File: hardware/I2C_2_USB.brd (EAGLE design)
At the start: 14.9 x 20.3 mm, 14 parts, among them CN1 1X4-BIG, J3 USB-MICROB, U1 ATMEGA328P-MU-QFN32

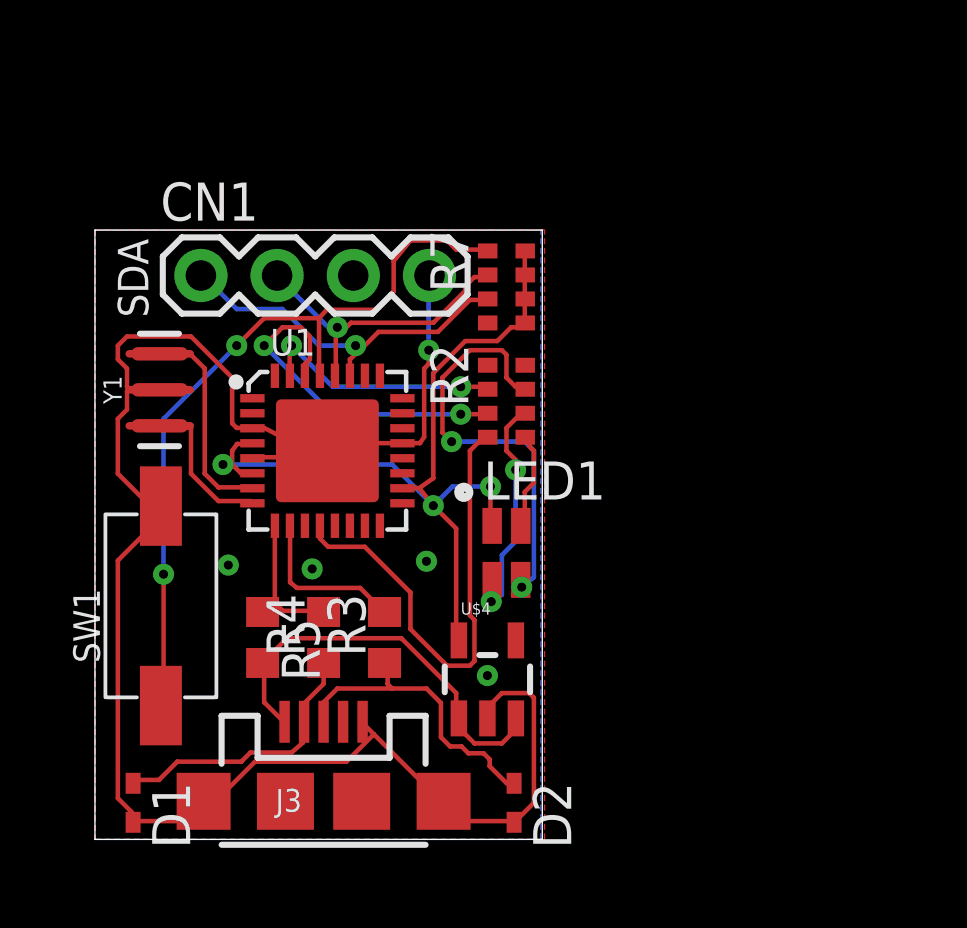
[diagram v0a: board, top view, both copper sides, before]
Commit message: Connect SDA and TxD Lines
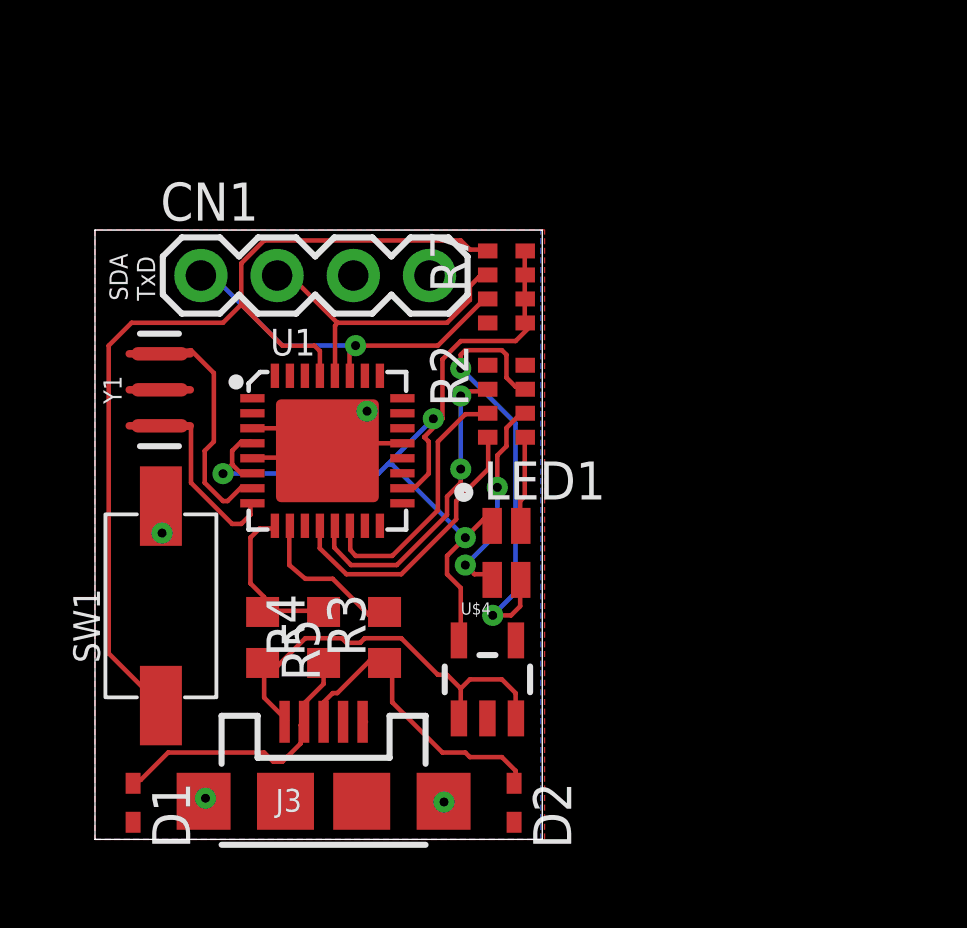
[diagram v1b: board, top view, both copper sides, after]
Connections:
- net LED renamed LED_RED
- removed net ADCENA: U1.13
- removed net OUTA: U1.14
- new net LED_BLUE: R2.3, U1.14
- new net LED_GREEN: R2.2, U1.13
- net RXD: no longer R2.3
- net TXD: no longer R2.2
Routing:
- net GND: track 60.3 -> 10.1 mm, vias 5 -> 4
- net RXD: track 11.7 -> 0.00 mm, vias 2 -> 0
- net LED_GREEN: track 0.00 -> 10.6 mm, vias 0 -> 2
- net LED_BLUE: track 0.00 -> 8.78 mm
- net TXD: track 8.29 -> 0.00 mm, vias 2 -> 0
- net LED_RED: track 16.0 -> 9.61 mm
- net RST: track 25.9 -> 31.9 mm, vias 2 -> 0
- net XTAL1: track 6.98 -> 7.95 mm
- net XTAL2: track 5.03 -> 5.96 mm
- net BLUE: track 7.87 -> 7.12 mm
- net +3V3: track 29.9 -> 30.4 mm
- net SCL: track 10.2 -> 10.4 mm, vias 1 -> 0
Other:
- board text added: "SDA TxD"
- board text removed: "SDA"

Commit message: Add crypto module & backside labels
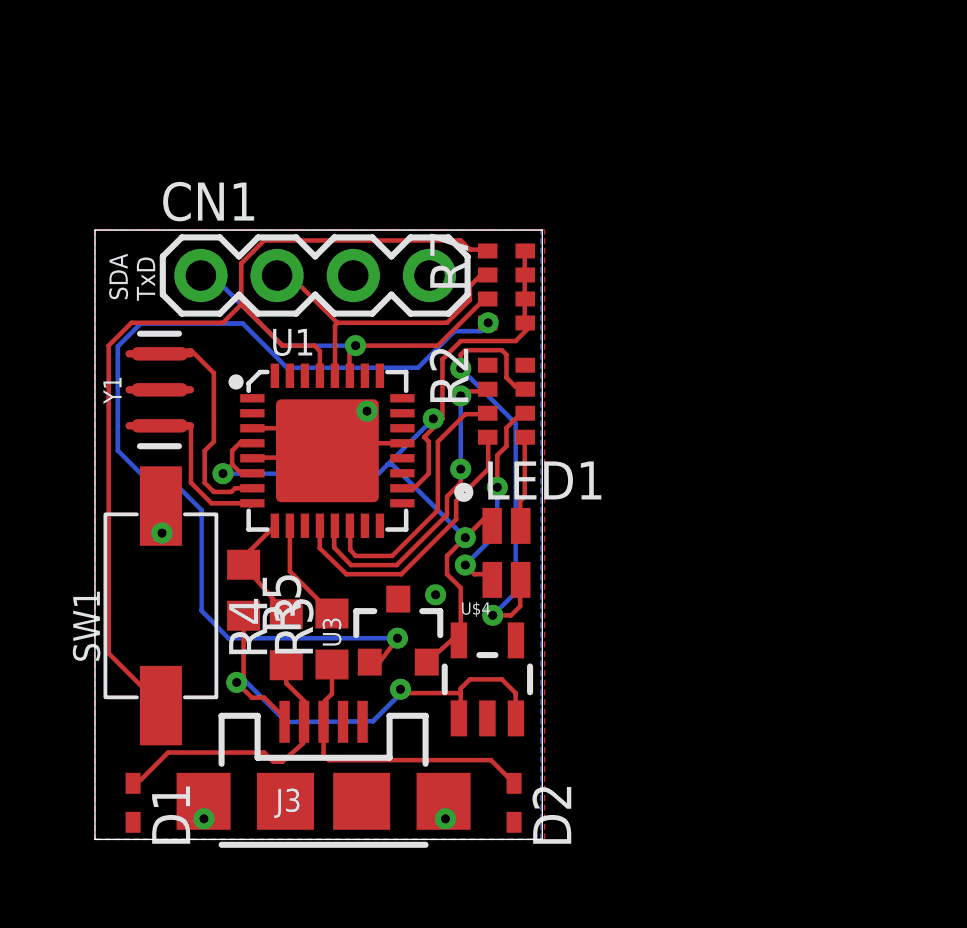
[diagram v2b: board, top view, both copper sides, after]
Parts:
- added U3: ATSHA204-TSU, SparkFun-IC-Special-Function:SOT23-3
- moved R3 1.75 mm to (7.90, 6.68)
- moved R5 1.70 mm to (4.95, 8.31)
- moved R4 1.25 mm to (6.38, 6.65)
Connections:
- new net CRYPTO: R7.4, U3.1
- net +3V3: now also U3.2
- net GND: now also U3.3
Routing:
- net CRYPTO: track 0.00 -> 33.0 mm, vias 0 -> 2
- net +5V: track 14.1 -> 17.2 mm, vias 0 -> 2
- net D-: track 5.71 -> 3.91 mm
- net D+: track 5.23 -> 3.50 mm
- net +3V3: track 30.4 -> 31.8 mm
- net XTAL2: track 5.96 -> 5.30 mm
- net GND: track 10.1 -> 9.46 mm, vias 4 -> 5
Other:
- board text added: "3V3"
- board text added: "GND"
- board text added: "SCL RxD"

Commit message: Add BLE module
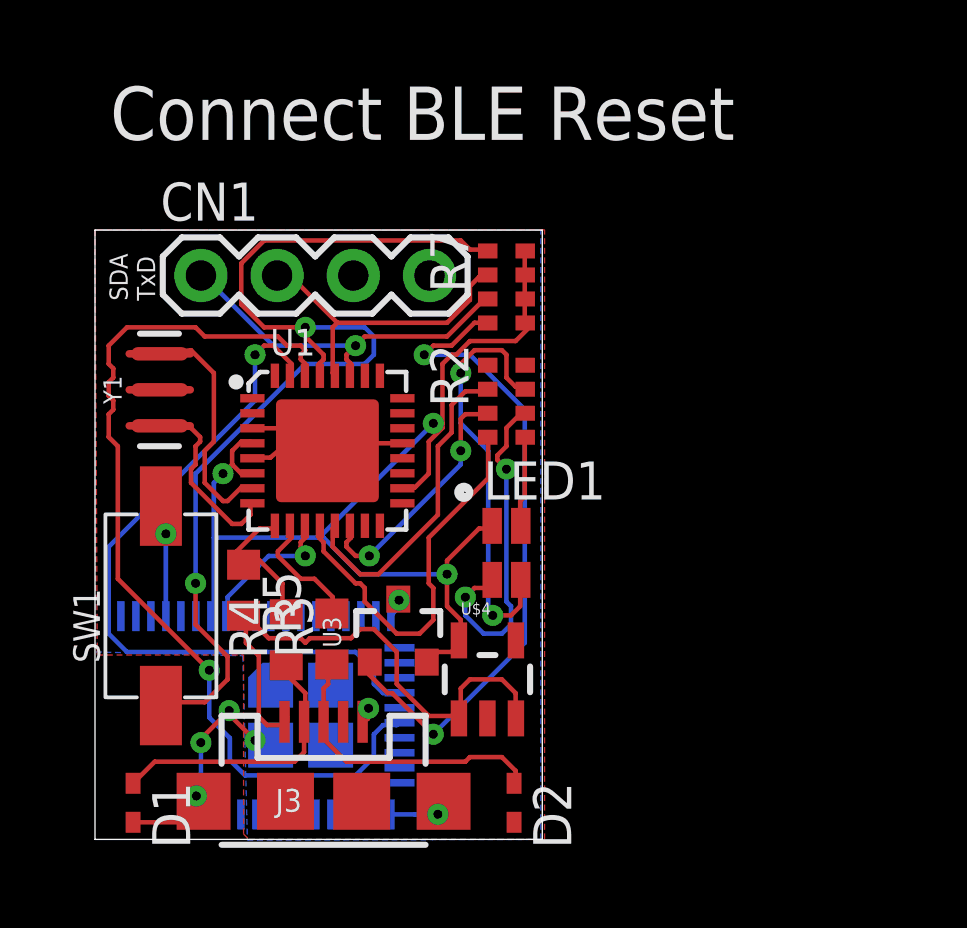
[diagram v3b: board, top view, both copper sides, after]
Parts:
- added U2: RFD77101, SparkFun-RF:RFD77101
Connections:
- removed net RADIO_ON: U1.11
- new net BLE_RESET: U1.11, U2.8
- net +3V3: now also U2.7
- net GND: now also U2.1, U2.19, U2.2, U2.30, U2.4, U2.42, U2.43, U2.44, U2.45, U2.6
- net RXD: now also U2.25
- net TXD: now also U2.23
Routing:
- net RXD: track 0.00 -> 30.9 mm, vias 0 -> 1
- net TXD: track 0.00 -> 24.1 mm, vias 0 -> 1
- net GND: track 9.46 -> 24.4 mm, vias 5 -> 8
- net CRYPTO: track 33.0 -> 22.1 mm
- net +3V3: track 31.8 -> 38.7 mm
- net BLE_RESET: track 0.00 -> 4.96 mm, vias 0 -> 1
- net BLUE: track 7.12 -> 11.4 mm
- net LED_RED: track 9.61 -> 13.1 mm
- net RST: track 31.9 -> 35.0 mm, vias 0 -> 2
- net +5V: track 17.2 -> 18.7 mm, vias 2 -> 0
- net D-: track 3.91 -> 4.95 mm
- net XTAL2: track 5.30 -> 6.21 mm
- net GREEN: track 14.9 -> 14.1 mm
- net D+: track 3.50 -> 4.16 mm
- net LED_BLUE: track 8.78 -> 8.46 mm, vias 0 -> 2
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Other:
- board text added: "Connect BLE Reset"
